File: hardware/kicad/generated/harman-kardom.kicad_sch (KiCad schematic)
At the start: 25 parts, among them J1 USB-C PD INPUT, J2 WOOFER / IMPEDANCE TBD, J3 TWEETER / IMPEDANCE TBD, SW1 FUNCTION / RESET / PROVISION, U1 USB-C PD TRIGGER / 20 V, U2 XL4015 CC/CV / 16.80 V 2.00 A, U3 4S BALANCED BMS / COMMON PORT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, U4 MP1584 / ADJUST TO 5.10 V, U5 ESP32-S3 N16R8 DEV BOARD, U6 PCM5102A I2S DAC MODULE, U7 XH-A232 / TPA3110 BTL AMP

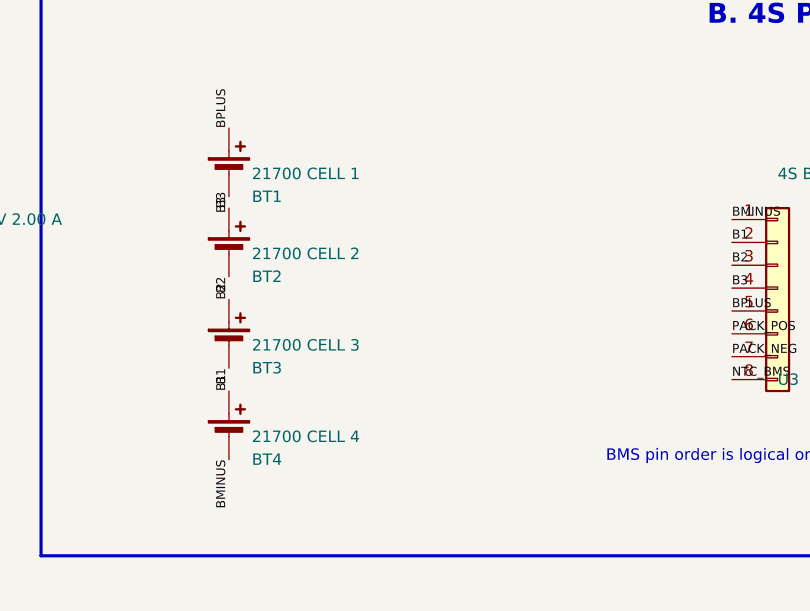
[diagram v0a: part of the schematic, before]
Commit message: docs: select Aspilsan cells and cheaper charger
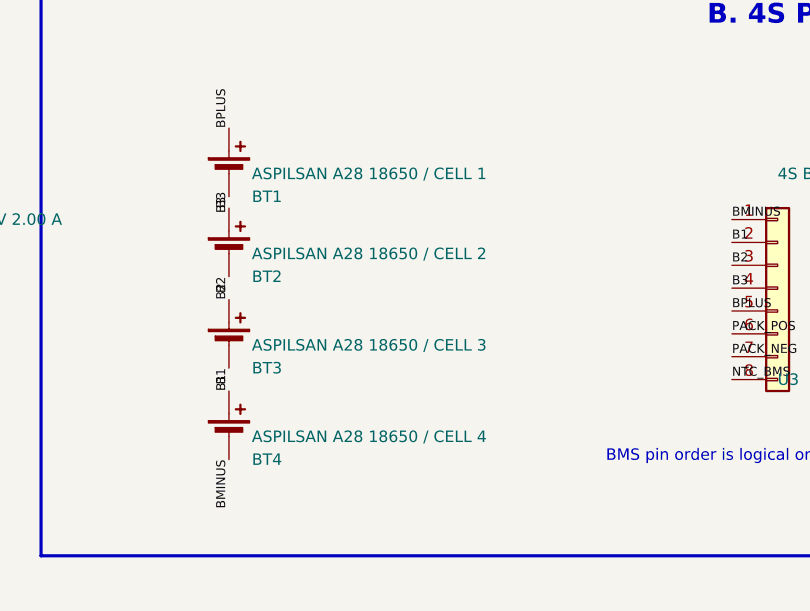
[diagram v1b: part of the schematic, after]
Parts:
- BT1: value 21700 CELL 1 -> ASPILSAN A28 18650 / CELL 1
- BT2: value 21700 CELL 2 -> ASPILSAN A28 18650 / CELL 2
- BT3: value 21700 CELL 3 -> ASPILSAN A28 18650 / CELL 3
- BT4: value 21700 CELL 4 -> ASPILSAN A28 18650 / CELL 4
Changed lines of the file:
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@@
 		(instances
 			(project "harman-kardom"
-				(path "/35029f4d-8913-4efc-88a2-aa253a2cd07a"
+				(path "/5ad5c568-c7e7-40fd-9fc8-742e45dff40d"
 					(reference "J1")
 					(unit 1)
@@
 		(instances
 			(project "harman-kardom"
-				(path "/35029f4d-8913-4efc-88a2-aa253a2cd07a"
+				(path "/5ad5c568-c7e7-40fd-9fc8-742e45dff40d"
 					(reference "U1")
 					(unit 1)
@@
 		(instances
 			(project "harman-kardom"
-				(path "/35029f4d-8913-4efc-88a2-aa253a2cd07a"
+				(path "/5ad5c568-c7e7-40fd-9fc8-742e45dff40d"
 					(reference "U2")
 					(unit 1)
@@
 		(instances
 			(project "harman-kardom"
-				(path "/35029f4d-8913-4efc-88a2-aa253a2cd07a"
+				(path "/5ad5c568-c7e7-40fd-9fc8-742e45dff40d"
 					(reference "U3")
 					(unit 1)
@@
 		(instances
 			(project "harman-kardom"
-				(path "/35029f4d-8913-4efc-88a2-aa253a2cd07a"
+				(path "/5ad5c568-c7e7-40fd-9fc8-742e45dff40d"
 					(reference "U4")
 					(unit 1)
@@
 		(instances
 			(project "harman-kardom"
-				(path "/35029f4d-8913-4efc-88a2-aa253a2cd07a"
+				(path "/5ad5c568-c7e7-40fd-9fc8-742e45dff40d"
 					(reference "JP1")
 					(unit 1)
@@
 		(instances
 			(project "harman-kardom"
-				(path "/35029f4d-8913-4efc-88a2-aa253a2cd07a"
+				(path "/5ad5c568-c7e7-40fd-9fc8-742e45dff40d"
 					(reference "U5")
 					(unit 1)
@@
 		(instances
 			(project "harman-kardom"
-				(path "/35029f4d-8913-4efc-88a2-aa253a2cd07a"
+				(path "/5ad5c568-c7e7-40fd-9fc8-742e45dff40d"
 					(reference "D1")
 					(unit 1)
@@
 		(instances
 			(project "harman-kardom"
-				(path "/35029f4d-8913-4efc-88a2-aa253a2cd07a"
+				(path "/5ad5c568-c7e7-40fd-9fc8-742e45dff40d"
 					(reference "U6")
 					(unit 1)
@@
 		(instances
 			(project "harman-kardom"
-				(path "/35029f4d-8913-4efc-88a2-aa253a2cd07a"
+				(path "/5ad5c568-c7e7-40fd-9fc8-742e45dff40d"
 					(reference "U7")
 					(unit 1)
@@
 		(instances
 			(project "harman-kardom"
-				(path "/35029f4d-8913-4efc-88a2-aa253a2cd07a"
+				(path "/5ad5c568-c7e7-40fd-9fc8-742e45dff40d"
 					(reference "J2")
 					(unit 1)
@@
 		(instances
 			(project "harman-kardom"
-				(path "/35029f4d-8913-4efc-88a2-aa253a2cd07a"
+				(path "/5ad5c568-c7e7-40fd-9fc8-742e45dff40d"
 					(reference "J3")
 					(unit 1)
@@
 		(instances
 			(project "harman-kardom"
-				(path "/35029f4d-8913-4efc-88a2-aa253a2cd07a"
+				(path "/5ad5c568-c7e7-40fd-9fc8-742e45dff40d"
 					(reference "JTP1")
 					(unit 1)
@@
 		(instances
 			(project "harman-kardom"
-				(path "/35029f4d-8913-4efc-88a2-aa253a2cd07a"
+				(path "/5ad5c568-c7e7-40fd-9fc8-742e45dff40d"
 					(reference "JTP2")
 					(unit 1)
@@
 		(instances
 			(project "harman-kardom"
-				(path "/35029f4d-8913-4efc-88a2-aa253a2cd07a"
+				(path "/5ad5c568-c7e7-40fd-9fc8-742e45dff40d"
 					(reference "JTP3")
 					(unit 1)
@@
 			)
 		)
-		(property "Value" "21700 CELL 1"
+		(property "Value" "ASPILSAN A28 18650 / CELL 1"
 			(at 185.42 35.56 0.0000)
 			(effects
@@
 		(instances
 			(project "harman-kardom"
-				(path "/35029f4d-8913-4efc-88a2-aa253a2cd07a"
+				(path "/5ad5c568-c7e7-40fd-9fc8-742e45dff40d"
 					(reference "BT1")
 					(unit 1)
@@
 			)
 		)
-		(property "Value" "21700 CELL 2"
+		(property "Value" "ASPILSAN A28 18650 / CELL 2"
 			(at 185.42 44.45 0.0000)
 			(effects
@@
 		(instances
 			(project "harman-kardom"
-				(path "/35029f4d-8913-4efc-88a2-aa253a2cd07a"
+				(path "/5ad5c568-c7e7-40fd-9fc8-742e45dff40d"
 					(reference "BT2")
 					(unit 1)
@@
 			)
 		)
-		(property "Value" "21700 CELL 3"
+		(property "Value" "ASPILSAN A28 18650 / CELL 3"
 			(at 185.42 54.61 0.0000)
 			(effects
@@
 		(instances
 			(project "harman-kardom"
-				(path "/35029f4d-8913-4efc-88a2-aa253a2cd07a"
+				(path "/5ad5c568-c7e7-40fd-9fc8-742e45dff40d"
 					(reference "BT3")
 					(unit 1)
@@
 			)
 		)
-		(property "Value" "21700 CELL 4"
+		(property "Value" "ASPILSAN A28 18650 / CELL 4"
 			(at 185.42 64.77 0.0000)
 			(effects
@@
 		(instances
 			(project "harman-kardom"
-				(path "/35029f4d-8913-4efc-88a2-aa253a2cd07a"
+				(path "/5ad5c568-c7e7-40fd-9fc8-742e45dff40d"
 					(reference "BT4")
 					(unit 1)
@@
 		(instances
 			(project "harman-kardom"
-				(path "/35029f4d-8913-4efc-88a2-aa253a2cd07a"
+				(path "/5ad5c568-c7e7-40fd-9fc8-742e45dff40d"
 					(reference "F1")
 					(unit 1)
@@
 		(instances
 			(project "harman-kardom"
-				(path "/35029f4d-8913-4efc-88a2-aa253a2cd07a"
+				(path "/5ad5c568-c7e7-40fd-9fc8-742e45dff40d"
 					(reference "S1")
 					(unit 1)
@@
 		(instances
 			(project "harman-kardom"
-				(path "/35029f4d-8913-4efc-88a2-aa253a2cd07a"
+				(path "/5ad5c568-c7e7-40fd-9fc8-742e45dff40d"
 					(reference "C1")
 					(unit 1)
@@
 		(instances
 			(project "harman-kardom"
-				(path "/35029f4d-8913-4efc-88a2-aa253a2cd07a"
+				(path "/5ad5c568-c7e7-40fd-9fc8-742e45dff40d"
 					(reference "SW1")
 					(unit 1)
@@
 		(instances
 			(project "harman-kardom"
-				(path "/35029f4d-8913-4efc-88a2-aa253a2cd07a"
+				(path "/5ad5c568-c7e7-40fd-9fc8-742e45dff40d"
 					(reference "R1")
 					(unit 1)
@@
 		(instances
 			(project "harman-kardom"
-				(path "/35029f4d-8913-4efc-88a2-aa253a2cd07a"
+				(path "/5ad5c568-c7e7-40fd-9fc8-742e45dff40d"
 					(reference "C2")
 					(unit 1)

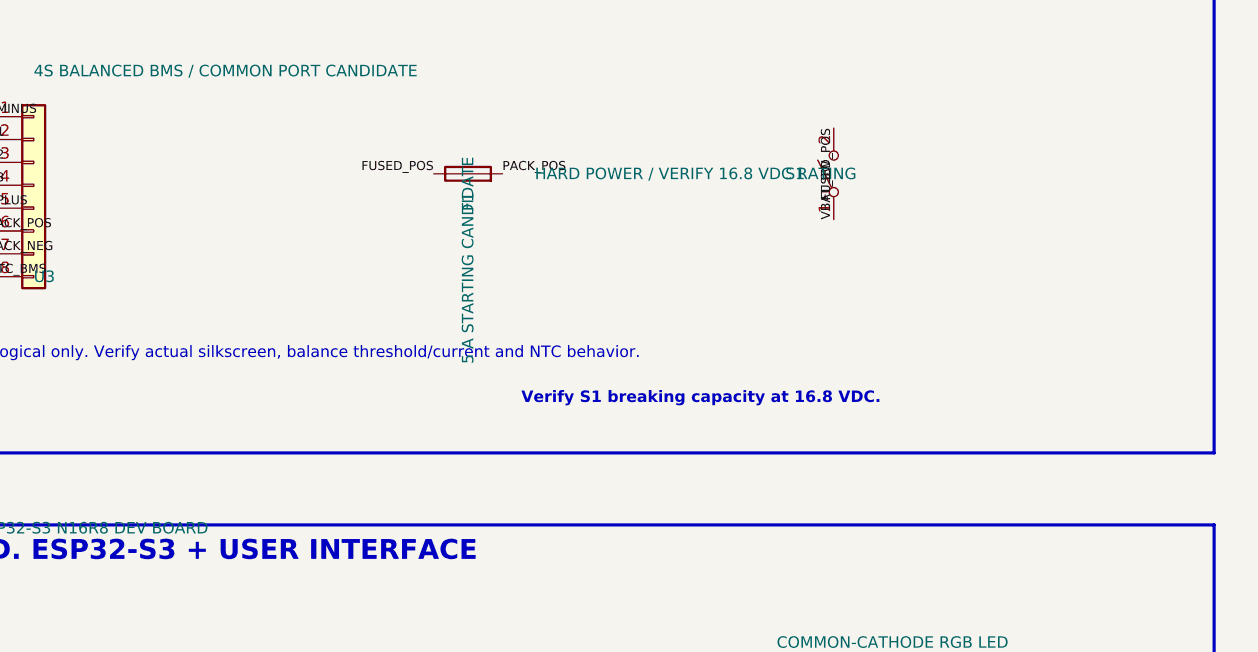
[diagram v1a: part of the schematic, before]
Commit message: docs: select KM103 power switch candidate
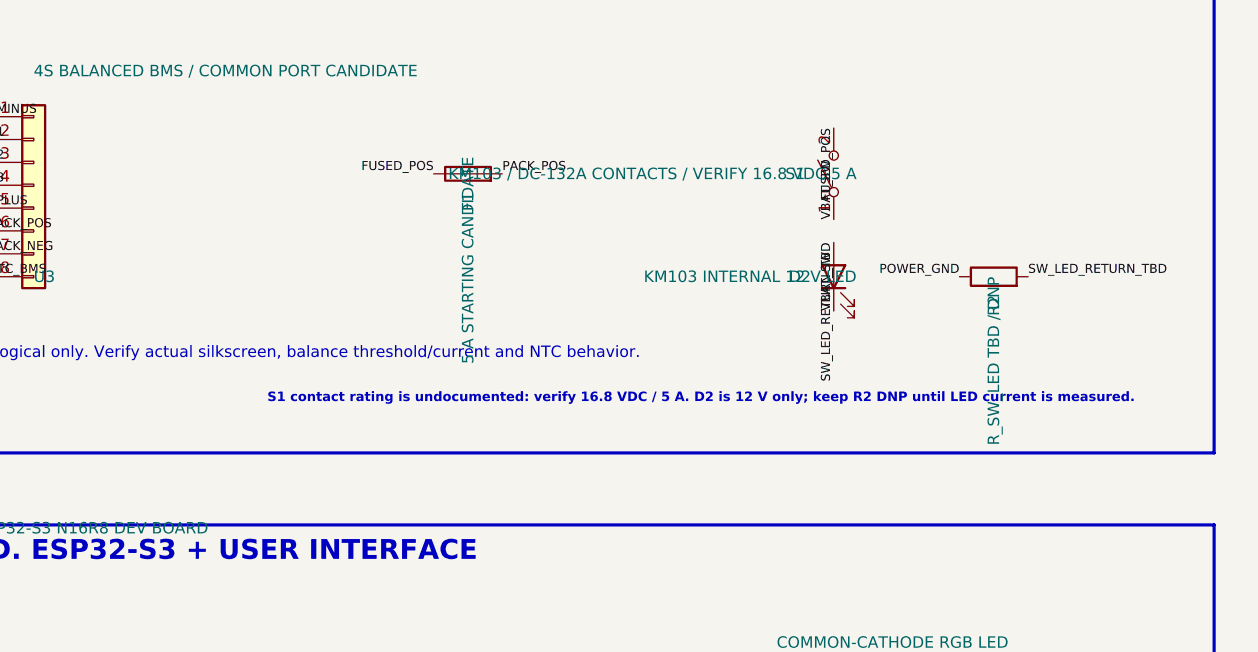
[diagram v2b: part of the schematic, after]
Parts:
- added D2: KM103 INTERNAL 12 V LED, symbol Device:LED
- added R2: R_SW_LED TBD / DNP, symbol Device:R
- S1: value HARD POWER / VERIFY 16.8 VDC RATING -> KM103 / DC-132A CONTACTS / VERIFY 16.8 VDC 5 A
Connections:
- net POWER_GND: now also R2.1
- net VBAT_SW: now also D2.1 (K)
- new net SW_LED_RETURN_TBD: D2.2 (A), R2.2
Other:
- note added: "S1 contact rating is undocumented: verify 16.8 VDC / 5 A. D2 is 12 V only; keep R2 DNP until LED current is measured."
- note removed: "Verify S1 breaking capacity at 16.8 VDC."
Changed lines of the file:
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@@
 		(title "Harman Kardom - Module-Level Prototype")
 		(date "2026-08-30")
-		(rev "0.4-candidate")
+		(rev "0.5-candidate")
 		(company "Harman Kardom")
 		(comment 1 "4S Li-ion / USB-C PD / ESP32-S3 / PCM5102A / XH-A232")
@@
 		(instances
 			(project "harman-kardom"
-				(path "/5ad5c568-c7e7-40fd-9fc8-742e45dff40d"
+				(path "/7a021c7b-2503-43bd-a4b3-4085f7ede911"
 					(reference "J1")
 					(unit 1)
@@
 		(instances
 			(project "harman-kardom"
-				(path "/5ad5c568-c7e7-40fd-9fc8-742e45dff40d"
+				(path "/7a021c7b-2503-43bd-a4b3-4085f7ede911"
 					(reference "U1")
 					(unit 1)
@@
 		(instances
 			(project "harman-kardom"
-				(path "/5ad5c568-c7e7-40fd-9fc8-742e45dff40d"
+				(path "/7a021c7b-2503-43bd-a4b3-4085f7ede911"
 					(reference "U2")
 					(unit 1)
@@
 		(instances
 			(project "harman-kardom"
-				(path "/5ad5c568-c7e7-40fd-9fc8-742e45dff40d"
+				(path "/7a021c7b-2503-43bd-a4b3-4085f7ede911"
 					(reference "U3")
 					(unit 1)
@@
 		(instances
 			(project "harman-kardom"
-				(path "/5ad5c568-c7e7-40fd-9fc8-742e45dff40d"
+				(path "/7a021c7b-2503-43bd-a4b3-4085f7ede911"
 					(reference "U4")
 					(unit 1)
@@
 		(instances
 			(project "harman-kardom"
-				(path "/5ad5c568-c7e7-40fd-9fc8-742e45dff40d"
+				(path "/7a021c7b-2503-43bd-a4b3-4085f7ede911"
 					(reference "JP1")
 					(unit 1)
@@
 		(instances
 			(project "harman-kardom"
-				(path "/5ad5c568-c7e7-40fd-9fc8-742e45dff40d"
+				(path "/7a021c7b-2503-43bd-a4b3-4085f7ede911"
 					(reference "U5")
 					(unit 1)
@@
 		(instances
 			(project "harman-kardom"
-				(path "/5ad5c568-c7e7-40fd-9fc8-742e45dff40d"
+				(path "/7a021c7b-2503-43bd-a4b3-4085f7ede911"
 					(reference "D1")
 					(unit 1)
@@
 		(instances
 			(project "harman-kardom"
-				(path "/5ad5c568-c7e7-40fd-9fc8-742e45dff40d"
+				(path "/7a021c7b-2503-43bd-a4b3-4085f7ede911"
 					(reference "U6")
 					(unit 1)
@@
 		(instances
 			(project "harman-kardom"
-				(path "/5ad5c568-c7e7-40fd-9fc8-742e45dff40d"
+				(path "/7a021c7b-2503-43bd-a4b3-4085f7ede911"
 					(reference "U7")
 					(unit 1)
@@
 		(instances
 			(project "harman-kardom"
-				(path "/5ad5c568-c7e7-40fd-9fc8-742e45dff40d"
+				(path "/7a021c7b-2503-43bd-a4b3-4085f7ede911"
 					(reference "J2")
 					(unit 1)
@@
 		(instances
 			(project "harman-kardom"
-				(path "/5ad5c568-c7e7-40fd-9fc8-742e45dff40d"
+				(path "/7a021c7b-2503-43bd-a4b3-4085f7ede911"
 					(reference "J3")
 					(unit 1)
@@
 		(instances
 			(project "harman-kardom"
-				(path "/5ad5c568-c7e7-40fd-9fc8-742e45dff40d"
+				(path "/7a021c7b-2503-43bd-a4b3-4085f7ede911"
 					(reference "JTP1")
 					(unit 1)
@@
 		(instances
 			(project "harman-kardom"
-				(path "/5ad5c568-c7e7-40fd-9fc8-742e45dff40d"
+				(path "/7a021c7b-2503-43bd-a4b3-4085f7ede911"
 					(reference "JTP2")
 					(unit 1)
@@
 		(instances
 			(project "harman-kardom"
-				(path "/5ad5c568-c7e7-40fd-9fc8-742e45dff40d"
+				(path "/7a021c7b-2503-43bd-a4b3-4085f7ede911"
 					(reference "JTP3")
 					(unit 1)
@@
 		(instances
 			(project "harman-kardom"
-				(path "/5ad5c568-c7e7-40fd-9fc8-742e45dff40d"
+				(path "/7a021c7b-2503-43bd-a4b3-4085f7ede911"
 					(reference "BT1")
 					(unit 1)
@@
 		(instances
 			(project "harman-kardom"
-				(path "/5ad5c568-c7e7-40fd-9fc8-742e45dff40d"
+				(path "/7a021c7b-2503-43bd-a4b3-4085f7ede911"
 					(reference "BT2")
 					(unit 1)
@@
 		(instances
 			(project "harman-kardom"
-				(path "/5ad5c568-c7e7-40fd-9fc8-742e45dff40d"
+				(path "/7a021c7b-2503-43bd-a4b3-4085f7ede911"
 					(reference "BT3")
 					(unit 1)
@@
 		(instances
 			(project "harman-kardom"
-				(path "/5ad5c568-c7e7-40fd-9fc8-742e45dff40d"
+				(path "/7a021c7b-2503-43bd-a4b3-4085f7ede911"
 					(reference "BT4")
 					(unit 1)
@@
 		(instances
 			(project "harman-kardom"
-				(path "/5ad5c568-c7e7-40fd-9fc8-742e45dff40d"
+				(path "/7a021c7b-2503-43bd-a4b3-4085f7ede911"
 					(reference "F1")
 					(unit 1)
@@
 			)
 		)
-		(property "Value" "HARD POWER / VERIFY 16.8 VDC RATING"
+		(property "Value" "KM103 / DC-132A CONTACTS / VERIFY 16.8 VDC 5 A"
 			(at 335.28 46.99 90)
 			(effects
@@
 		(instances
 			(project "harman-kardom"
-				(path "/5ad5c568-c7e7-40fd-9fc8-742e45dff40d"
+				(path "/7a021c7b-2503-43bd-a4b3-4085f7ede911"
 					(reference "S1")
+					(unit 1)
+				)
+			)
+		)
+	)
+	(symbol
+		(lib_id "Device:LED")
+		(at 332.74 58.42 90)
+		(unit 1)
+		(exclude_from_sim no)
+		(in_bom yes)
+		(on_board yes)
+		(dnp no)
+		(fields_autoplaced no)
+		(property "Reference" "D2"
+			(at 330.2 58.42 90)
+			(effects
+				(font
+					(size 1.27 1.27)
+				)
+				(justify left)
+			)
+		)
+		(property "Value" "KM103 INTERNAL 12 V LED"
+			(at 335.28 58.42 90)
+			(effects
+				(font
+					(size 1.27 1.27)
+				)
+				(justify left)
+			)
+		)
+		(pin "1"
+		)
+		(pin "2"
+		)
+		(instances
+			(project "harman-kardom"
+				(path "/7a021c7b-2503-43bd-a4b3-4085f7ede911"
+					(reference "D2")
+					(unit 1)
+				)
+			)
+		)
+	)
+	(symbol
+		(lib_id "Device:R")
+		(at 350.52 58.42 90)
+		(unit 1)
+		(exclude_from_sim no)
+		(in_bom yes)
+		(on_board yes)
+		(dnp no)
+		(fields_autoplaced no)
+		(property "Reference" "R2"
+			(at 350.52 60.452 180)
+			(effects
+				(font
+					(size 1.27 1.27)
+				)
+				(justify left)
+			)
+		)
+		(property "Value" "R_SW_LED TBD / DNP"
+			(at 350.52 58.42 180)
+			(effects
+				(font
+					(size 1.27 1.27)
+				)
+				(justify left)
+			)
+		)
+		(pin "1"
+		)
+		(pin "2"
+		)
+		(instances
+			(project "harman-kardom"
+				(path "/7a021c7b-2503-43bd-a4b3-4085f7ede911"
+					(reference "R2")
 					(unit 1)
 				)
@@
 		(instances
 			(project "harman-kardom"
-				(path "/5ad5c568-c7e7-40fd-9fc8-742e45dff40d"
+				(path "/7a021c7b-2503-43bd-a4b3-4085f7ede911"
 					(reference "C1")
 					(unit 1)
@@
 		(instances
 			(project "harman-kardom"
-				(path "/5ad5c568-c7e7-40fd-9fc8-742e45dff40d"
+				(path "/7a021c7b-2503-43bd-a4b3-4085f7ede911"
 					(reference "SW1")
 					(unit 1)
@@
 		(instances
 			(project "harman-kardom"
-				(path "/5ad5c568-c7e7-40fd-9fc8-742e45dff40d"
+				(path "/7a021c7b-2503-43bd-a4b3-4085f7ede911"
 					(reference "R1")
 					(unit 1)
@@
 		(instances
 			(project "harman-kardom"
-				(path "/5ad5c568-c7e7-40fd-9fc8-742e45dff40d"
+				(path "/7a021c7b-2503-43bd-a4b3-4085f7ede911"
 					(reference "C2")
 					(unit 1)
@@
 			)
 			(justify left bottom)
+		)
+	)
+	(label "VBAT_SW"
+		(at 332.74 62.23 90)
+		(effects
+			(font
+				(size 1 1)
+			)
+			(justify left bottom)
+		)
+	)
+	(label "SW_LED_RETURN_TBD"
+		(at 332.74 54.61 270)
+		(effects
+			(font
+				(size 1 1)
+			)
+			(justify right bottom)
+		)
+	)
+	(label "SW_LED_RETURN_TBD"
+		(at 354.33 58.42 180)
+		(effects
+			(font
+				(size 1 1)
+			)
+			(justify left bottom)
+		)
+	)
+	(label "POWER_GND"
+		(at 346.71 58.42 0.0000)
+		(effects
+			(font
+				(size 1 1)
+			)
+			(justify right bottom)
 		)
 	)
@@
 		)
 	)
-	(text "Verify S1 breaking capacity at 16.8 VDC."
+	(text "S1 contact rating is undocumented: verify 16.8 VDC / 5 A. D2 is 12 V only; keep R2 DNP until LED current is measured."
 		(exclude_from_sim no)
 		(at 318 72 0.0000)
 		(effects
 			(font
-				(size 1.27 1.27)
+				(size 1.05 1.05)
 				(bold yes)
 			)
